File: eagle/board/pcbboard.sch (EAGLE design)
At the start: 39 parts, among them U2 ATMEGA328P-PU, Y2 16MHz

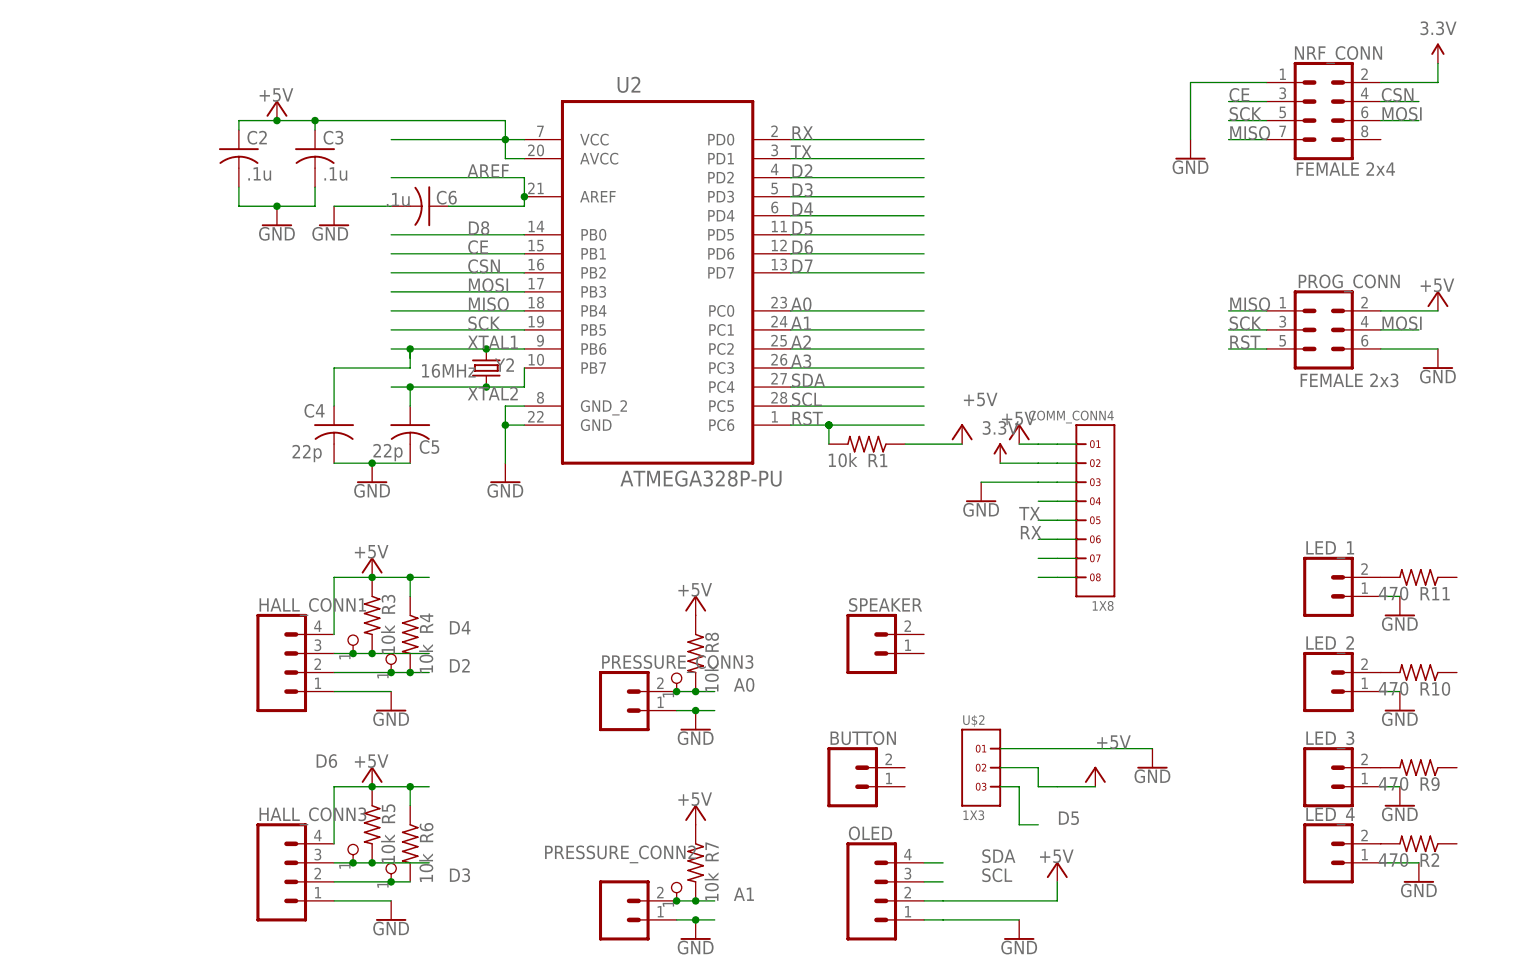
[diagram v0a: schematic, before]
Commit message: Re organized board
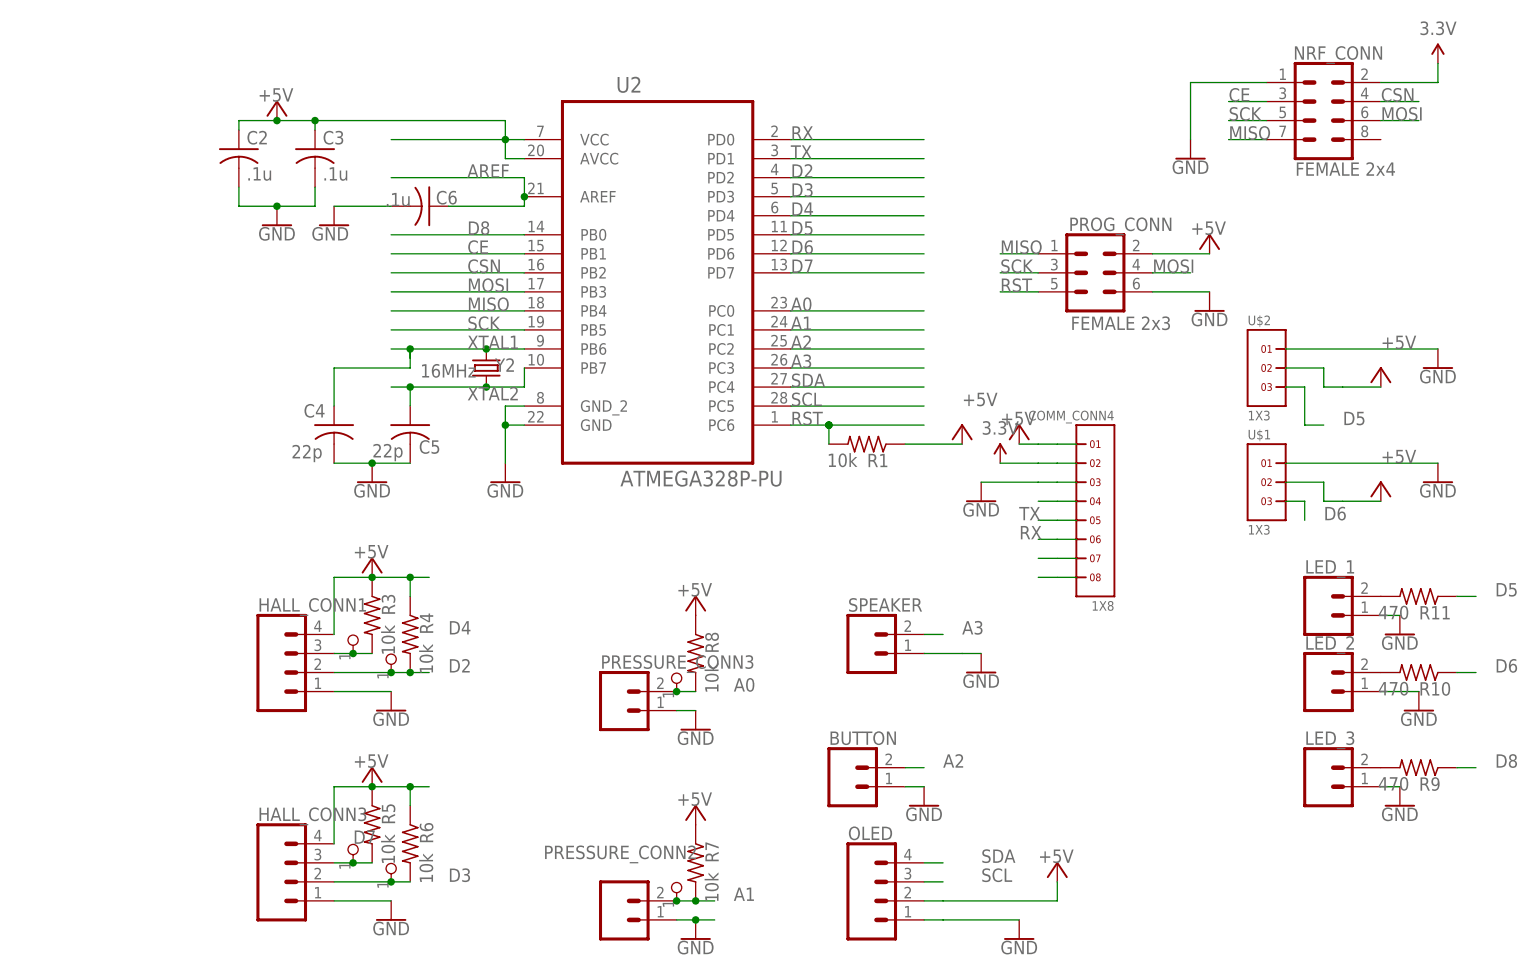
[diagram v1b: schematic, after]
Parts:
- removed LED_4: (no value), SparkFun-Connectors:CONN_02
- removed R2: 470, rcl:R-US_R0805
- added U$1: 1X3, headers(2mm):1X3
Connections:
- removed net N$2: LED_4.2, R2.2
- net +5V: now also U$1.2
- net A2: now also BUTTON.2
- net A3: now also SPEAKER.2
- net D5: now also R11.1
- net D6: now also R10.1, U$1.3; no longer HALL_CONN3.3, NO_NAME4.1, R5.2
- net D7: now also HALL_CONN3.3, NO_NAME4.1, R5.2
- net D8: now also R9.1
- net GND: now also BUTTON.1, SPEAKER.1, U$1.1; no longer LED_4.1
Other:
- moved on the sheet: LED_1, PROG_CONN, R11, U$2

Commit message: CLeaned up layout board
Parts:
- removed HALL_CONN1, HALL_CONN3: (no value), SparkFun-Connectors:CONN_04PTH
- removed PRESSURE_CONN2, PRESSURE_CONN3: (no value), SparkFun-Connectors:CONN_02
- added FORCE_1, FORCE_2: JST-XH-02-PIN-ROUND-PAD, Rembrandt Electronics - JST XH Connectors v1-0:JST-XH-02-PIN-ROUND-PAD
- added HALL_1, HALL_2: JST-XH-04-PIN-ROUND-PAD, Rembrandt Electronics - JST XH Connectors v1-0:JST-XH-04-PIN-ROUND-PAD
- added TP_3.3V, TP_5V: (no value), pinhead:PINHD-1X1
- BUTTON, LED_1, LED_2, LED_3, SPEAKER: value (none) -> JST-XH-02-PIN-ROUND-PAD; device SparkFun-Connectors:CONN_02 -> Rembrandt Electronics - JST XH Connectors v1-0:JST-XH-02-PIN-ROUND-PAD
- OLED: value (none) -> JST-XH-04-PIN-ROUND-PAD; device SparkFun-Connectors:CONN_04PTH -> Rembrandt Electronics - JST XH Connectors v1-0:JST-XH-04-PIN-ROUND-PAD
- renumbered NO_NAME to TP_F1, NO_NAME1 to TP_H1-2, NO_NAME2 to TP_H1-1, NO_NAME3 to TP_H2-2, NO_NAME4 to TP_H2-1, NO_NAME5 to TP_F2
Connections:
- removed net N$6: LED_2.2, R10.2
- removed net N$7: LED_1.2, R11.2
- new net N$2: LED_3-2.S, R9.2
- new net N$4: LED_1-2.S, R11.2
- net +5V: now also HALL_1-4.S, HALL_2-4.S, OLED-2.S, TP_5V.1; no longer HALL_CONN1.4, HALL_CONN3.4, OLED.2
- net 3.3V: now also TP_3.3V.1
- net A0: now also FORCE_1-2.S; no longer PRESSURE_CONN3.2
- net A1: now also FORCE_2-2.S; no longer PRESSURE_CONN2.2
- net A2: now also SPEAKER-2.S; no longer BUTTON.2
- net A3: now also BUTTON-2.S; no longer SPEAKER.2
- net D2: now also HALL_1-2.S; no longer HALL_CONN1.2
- net D3: now also HALL_2-2.S; no longer HALL_CONN3.2
- net D4: now also HALL_1-3.S; no longer HALL_CONN1.3
- net D7: now also HALL_2-3.S; no longer HALL_CONN3.3
- net GND: now also BUTTON-1.S, FORCE_1-1.S, FORCE_2-1.S, HALL_1-1.S, HALL_2-1.S, LED_1-1.S, LED_2-1.S, LED_3-1.S, OLED-1.S, SPEAKER-1.S; no longer BUTTON.1, HALL_CONN1.1, HALL_CONN3.1, LED_1.1, LED_2.1, LED_3.1, OLED.1, PRESSURE_CONN2.1, PRESSURE_CONN3.1, SPEAKER.1
- net N$3: now also LED_2-2.S, R10.2; no longer LED_3.2, R9.2
- net SCL: now also OLED-3.S; no longer OLED.3
- net SDA: now also OLED-4.S; no longer OLED.4
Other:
- note added: "Hall 1"
- note added: "Weight 1"

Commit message: Remote almost finish
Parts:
- removed C6: .1u, rcl:C-USC0805
- removed U2: ATMEGA328P-PU, Atmel_By_element14_Batch_1-00:ATMEGA328P-PU
- removed Y2: 16MHz, SparkFun-Clocks:CRYSTAL-8MHZSMD-5X3.2
- added 3.3V, 5V: (no value), adafruit:LED3MM
- added C1: .1u, rcl:C-USC0805
- added R12, R2: 470, rcl:R-US_R0805
- added RX_EN, TX_EN: (no value), SparkFun-Connectors:CONN_02
- added U1: ATMEGA328P-PU, Atmel_By_element14_Batch_1-00:ATMEGA328P-PU
- added Y1: 16MHz, SparkFun-Clocks:CRYSTAL-8MHZSMD-5X3.2
- R10, R11: value 470 -> 10k
- R7, R8: value 10k -> 470
- renumbered U$1 to X3, U$2 to X2
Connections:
- new net N$10: RX_EN.1, U1.PD0
- new net N$11: TX_EN.1, U1.PD1
- new net N$6: 3.3V.C, R2.1
- new net N$7: 5V.C, R12.1
- net +5V: now also 5V.A, C1.1, R10.1, R11.1, U1.AVCC, U1.VCC; no longer C3.1, R7.1, R8.1, U2.AVCC, U2.VCC
- net 3.3V: now also 3.3V.A
- net A0: now also R5.2, U1.PC0; no longer R8.2, U2.PC0
- net A1: now also R10.2, U1.PC1; no longer R7.2, U2.PC1
- net A2: now also U1.PC2; no longer U2.PC2
- net A3: now also U1.PC3; no longer U2.PC3
- net AREF: now also C3.1, U1.AREF; no longer C6.1, U2.AREF
- net CE: now also U1.PB1; no longer U2.PB1
- net CSN: now also U1.PB2; no longer U2.PB2
- net D2: now also U1.PD2; no longer U2.PD2
- net D3: now also R11.2, U1.PD3; no longer R6.2, U2.PD3
- net D4: now also U1.PD4; no longer U2.PD4
- net D5: now also R9.1, U1.PD5; no longer R11.1, U2.PD5
- net D6: now also R8.1, U1.PD6; no longer R10.1, U2.PD6
- net D7: now also R6.2, U1.PD7; no longer R5.2, U2.PD7
- net D8: now also R7.1, U1.PB0; no longer R9.1, U2.PB0
- net GND: now also C1.2, R12.2, R2.2, U1.GND, U1.GND_2; no longer C6.2, U2.GND, U2.GND_2
- net MISO: now also U1.PB4; no longer U2.PB4
- net MOSI: now also U1.PB3; no longer U2.PB3
- net N$2: now also R7.2; no longer R9.2
- net N$3: now also R8.2; no longer R10.2
- net N$4: now also R9.2; no longer R11.2
- net RST: now also U1.PC6; no longer U2.PC6
- net RX: now also RX_EN.2; no longer U2.PD0
- net SCK: now also U1.PB5; no longer U2.PB5
- net SCL: now also U1.PC5; no longer U2.PC5
- net SDA: now also U1.PC4; no longer U2.PC4
- net TX: now also TX_EN.2; no longer U2.PD1
- net XTAL1: now also U1.PB6, Y1.1; no longer U2.PB6, Y2.1
- net XTAL2: now also U1.PB7, Y1.2; no longer U2.PB7, Y2.2
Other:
- moved on the sheet: C2, C3, C4, C5, NRF_CONN, PROG_CONN, R1, R10, R11, R5, R6, R7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
